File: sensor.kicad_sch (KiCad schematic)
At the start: 135 parts, among them IC1 A3909, J1 Micro_SD_Card_Det1, J12 Conn_01x04, J13 1x3 servo, J14 1x3 servo, J15 arming terminal, J16 arming terminal, J17 arming terminal, J18 arming terminal, J19 Screw_Terminal_01x02, J20 Screw_Terminal_01x02, J21 Screw_Terminal_01x02, J22 Screw_Terminal_01x02, J3 Conn_Coaxial, J4 H9161TR-ND, J5 Screw_Term, J6 1x3 servo, J9 1x3 servo, Q1 2N7002, Q10 2N7002, Q11 2N7002, Q12 2N7002, Q13 2N7002, Q3 2N7002, Q4 2N7002, Q5 2N7002, Q6 2N7002, Q7 BSS138, U10 LSM6DS3, U2 IMU, U5 LPS22HB, U6 GPS, U7 SX1276, U8 NAND, Y2 32.768kHz

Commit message: Added GPS footprint
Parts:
- U6: footprint L96-M33:XCVR_L96-M33 -> RF_GPS:Quectel_L96
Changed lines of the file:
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@@
 			)
 		)
-		(property "Footprint" "L96-M33:XCVR_L96-M33"
+		(property "Footprint" "RF_GPS:Quectel_L96"
 			(at 71.12 54.61 0)
 			(effects
@@
 			(at 71.12 54.61 0)
 			(effects
+				(font
+					(size 1.27 1.27)
+				)
+				(hide yes)
+			)
+		)
+		(property "Sim.Name" "<unknown>"
+			(at 71.12 54.61 0)
+			(effects

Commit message: i fogro
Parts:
- removed Q1, Q10, Q11, Q12, Q13, Q3, Q4, Q5, Q6: 2N7002, Package_TO_SOT_SMD:SOT-23, symbol Transistor_FET:2N7002
- added Q1, Q10, Q11, Q3, Q4, Q5, Q6, Q8, Q9: IRLML6402, Package_TO_SOT_SMD:SOT-23, symbol Transistor_FET:IRLML6402
- J1: footprint (none) -> Connector_Card:microSD_HC_Hirose_DM3D-SF
- J12: footprint (none) -> Connector_PinSocket_2.54mm:PinSocket_1x04_P2.54mm_Vertical
- J15, J16, J17, J18, J19, J20, J21, J22, J5: footprint (none) -> TerminalBlock_Phoenix:TerminalBlock_Phoenix_MKDS-1,5-2-5.08_1x02_P5.08mm_Horizontal
- Y2: footprint (none) -> Crystal:Crystal_SMD_0603-2Pin_6.0x3.5mm
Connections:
- net at R83.2: now also Q10.1 (G)
- net at R63.2: now also Q1.1 (G)
- net at J14.2 (Pin_2): now also Q1.2 (S)
- net at R68.2: now also Q1.3 (D)
- net at D4.1 (K), J20.1 (Pin_1): now also Q9.2 (S)
- net at R85.2: now also Q11.1 (G)
- net at D6.1 (K), J22.1 (Pin_1): now also Q11.2 (S)
- net at R61.2, R84.2: now also Q11.3 (D)
- net at R65.2: now also Q4.1 (G)
- net at J6.2 (Pin_2): now also Q4.2 (S)
- net at R70.2: now also Q4.3 (D)
- net at R64.2: now also Q3.1 (G)
- net at J13.2 (Pin_2): now also Q3.2 (S)
- net at R69.2: now also Q3.3 (D)
- net at D5.1 (K), J21.1 (Pin_1): now also Q10.2 (S)
- net at R60.2, R82.2: now also Q10.3 (D)
- net at R59.2, R80.2: now also Q9.3 (D)
- net at R66.2: now also Q5.1 (G)
- net at R67.2: now also Q6.1 (G)
- net at R79.2: now also Q8.1 (G)
- net at R71.2: now also Q5.3 (D)
- net at R62.2: now also Q6.3 (D)
- net at D3.1 (K), J19.1 (Pin_1): now also Q8.2 (S)
- net at R58.2, R78.2: now also Q8.3 (D)
- net at R81.2: now also Q9.1 (G)
- net at 1x3servo1.2 (Pin_2): now also Q6.2 (S)
- net at J9.2 (Pin_2): now also Q5.2 (S)

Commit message: started pcb
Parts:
- C14, C15, C18, C19, C20, C21, C22, C23, C24, C25, C26, C44, C45, C46, C47, C48, C49, C50, C51, C52, C53, C54, C55, C56, C57, C58: footprint Capacitor_SMD:C_0201_0603Metric -> Capacitor_SMD:C_0603_1608Metric
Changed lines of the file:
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@@
 			)
 		)
-		(property "Footprint" "Capacitor_SMD:C_0201_0603Metric"
+		(property "Footprint" "Capacitor_SMD:C_0603_1608Metric"
 			(at 116.84 145.0848 0)
 			(effects
@@
 			)
 		)
-		(property "Footprint" "Capacitor_SMD:C_0201_0603Metric"
+		(property "Footprint" "Capacitor_SMD:C_0603_1608Metric"
 			(at 342.9 32.7152 0)
 			(effects
@@
 			)
 		)
-		(property "Footprint" "Capacitor_SMD:C_0201_0603Metric"
+		(property "Footprint" "Capacitor_SMD:C_0603_1608Metric"
 			(at 116.84 134.9248 0)
 			(effects
@@
 			)
 		)
-		(property "Footprint" "Capacitor_SMD:C_0201_0603Metric"
+		(property "Footprint" "Capacitor_SMD:C_0603_1608Metric"
 			(at 91.44 117.1448 0)
 			(effects
@@
 			)
 		)
-		(property "Footprint" "Capacitor_SMD:C_0201_0603Metric"
+		(property "Footprint" "Capacitor_SMD:C_0603_1608Metric"
 			(at -2.2352 175.26 0)
 			(effects
@@
 			)
 		)
-		(property "Footprint" "Capacitor_SMD:C_0201_0603Metric"
+		(property "Footprint" "Capacitor_SMD:C_0603_1608Metric"
 			(at 37.7952 165.1 0)
 			(effects
@@
 			)
 		)
-		(property "Footprint" "Capacitor_SMD:C_0201_0603Metric"
+		(property "Footprint" "Capacitor_SMD:C_0603_1608Metric"
 			(at 91.44 120.3452 0)
 			(effects
@@
 			)
 		)
-		(property "Footprint" "Capacitor_SMD:C_0201_0603Metric"
+		(property "Footprint" "Capacitor_SMD:C_0603_1608Metric"
 			(at 270.51 36.83 0)
 			(effects
@@
 			)
 		)
-		(property "Footprint" "Capacitor_SMD:C_0201_0603Metric"
+		(property "Footprint" "Capacitor_SMD:C_0603_1608Metric"
 			(at 105.1052 34.29 0)
 			(effects
@@
 			)
 		)
-		(property "Footprint" "Capacitor_SMD:C_0201_0603Metric"
+		(property "Footprint" "Capacitor_SMD:C_0603_1608Metric"
 			(at 280.67 39.37 0)
 			(effects
@@
 			)
 		)
-		(property "Footprint" "Capacitor_SMD:C_0201_0603Metric"
+		(property "Footprint" "Capacitor_SMD:C_0603_1608Metric"
 			(at 193.04 127.3048 0)
 			(effects
@@
 			)
 		)
-		(property "Footprint" "Capacitor_SMD:C_0201_0603Metric"
+		(property "Footprint" "Capacitor_SMD:C_0603_1608Metric"
 			(at 91.44 122.2248 0)
 			(effects
@@
 			)
 		)
-		(property "Footprint" "Capacitor_SMD:C_0201_0603Metric"
+		(property "Footprint" "Capacitor_SMD:C_0603_1608Metric"
 			(at 266.3952 27.94 0)
 			(effects
@@
 			)
 		)
-		(property "Footprint" "Capacitor_SMD:C_0201_0603Metric"
+		(property "Footprint" "Capacitor_SMD:C_0603_1608Metric"
 			(at 229.87 89.8652 0)
 			(effects
@@
 			)
 		)
-		(property "Footprint" "Capacitor_SMD:C_0201_0603Metric"
+		(property "Footprint" "Capacitor_SMD:C_0603_1608Metric"
 			(at 229.87 84.7852 0)
 			(effects
@@
 			)
 		)
-		(property "Footprint" "Capacitor_SMD:C_0201_0603Metric"
+		(property "Footprint" "Capacitor_SMD:C_0603_1608Metric"
 			(at 91.44 125.4252 0)
 			(effects
@@
 			)
 		)
-		(property "Footprint" "Capacitor_SMD:C_0201_0603Metric"
+		(property "Footprint" "Capacitor_SMD:C_0603_1608Metric"
 			(at 93.98 42.8752 0)
 			(effects
@@
 			)
 		)
-		(property "Footprint" "Capacitor_SMD:C_0201_0603Metric"
+		(property "Footprint" "Capacitor_SMD:C_0603_1608Metric"
 			(at 127.3048 160.02 0)
 			(effects
@@
 			)
 		)
-		(property "Footprint" "Capacitor_SMD:C_0201_0603Metric"
+		(property "Footprint" "Capacitor_SMD:C_0603_1608Metric"
 			(at 114.3 159.0548 0)
 			(effects
@@
 			)
 		)
-		(property "Footprint" "Capacitor_SMD:C_0201_0603Metric"
+		(property "Footprint" "Capacitor_SMD:C_0603_1608Metric"
 			(at 340.36 30.7848 0)
 			(effects
@@
 			)
 		)
-		(property "Footprint" "Capacitor_SMD:C_0201_0603Metric"
+		(property "Footprint" "Capacitor_SMD:C_0603_1608Metric"
 			(at 262.89 51.7652 0)
 			(effects
@@
 			)
 		)
-		(property "Footprint" "Capacitor_SMD:C_0201_0603Metric"
+		(property "Footprint" "Capacitor_SMD:C_0603_1608Metric"
 			(at 271.4752 27.94 0)
 			(effects
@@
 			)
 		)
-		(property "Footprint" "Capacitor_SMD:C_0201_0603Metric"
+		(property "Footprint" "Capacitor_SMD:C_0603_1608Metric"
 			(at 116.84 140.0048 0)
 			(effects
@@
 			)
 		)
-		(property "Footprint" "Capacitor_SMD:C_0201_0603Metric"
+		(property "Footprint" "Capacitor_SMD:C_0603_1608Metric"
 			(at 91.44 115.2652 0)
 			(effects
@@
 			)
 		)
-		(property "Footprint" "Capacitor_SMD:C_0201_0603Metric"
+		(property "Footprint" "Capacitor_SMD:C_0603_1608Metric"
 			(at 117.8052 36.83 0)
 			(effects
@@
 			)
 		)
-		(property "Footprint" "Capacitor_SMD:C_0201_0603Metric"
+		(property "Footprint" "Capacitor_SMD:C_0603_1608Metric"
 			(at 116.84 150.1648 0)
 			(effects

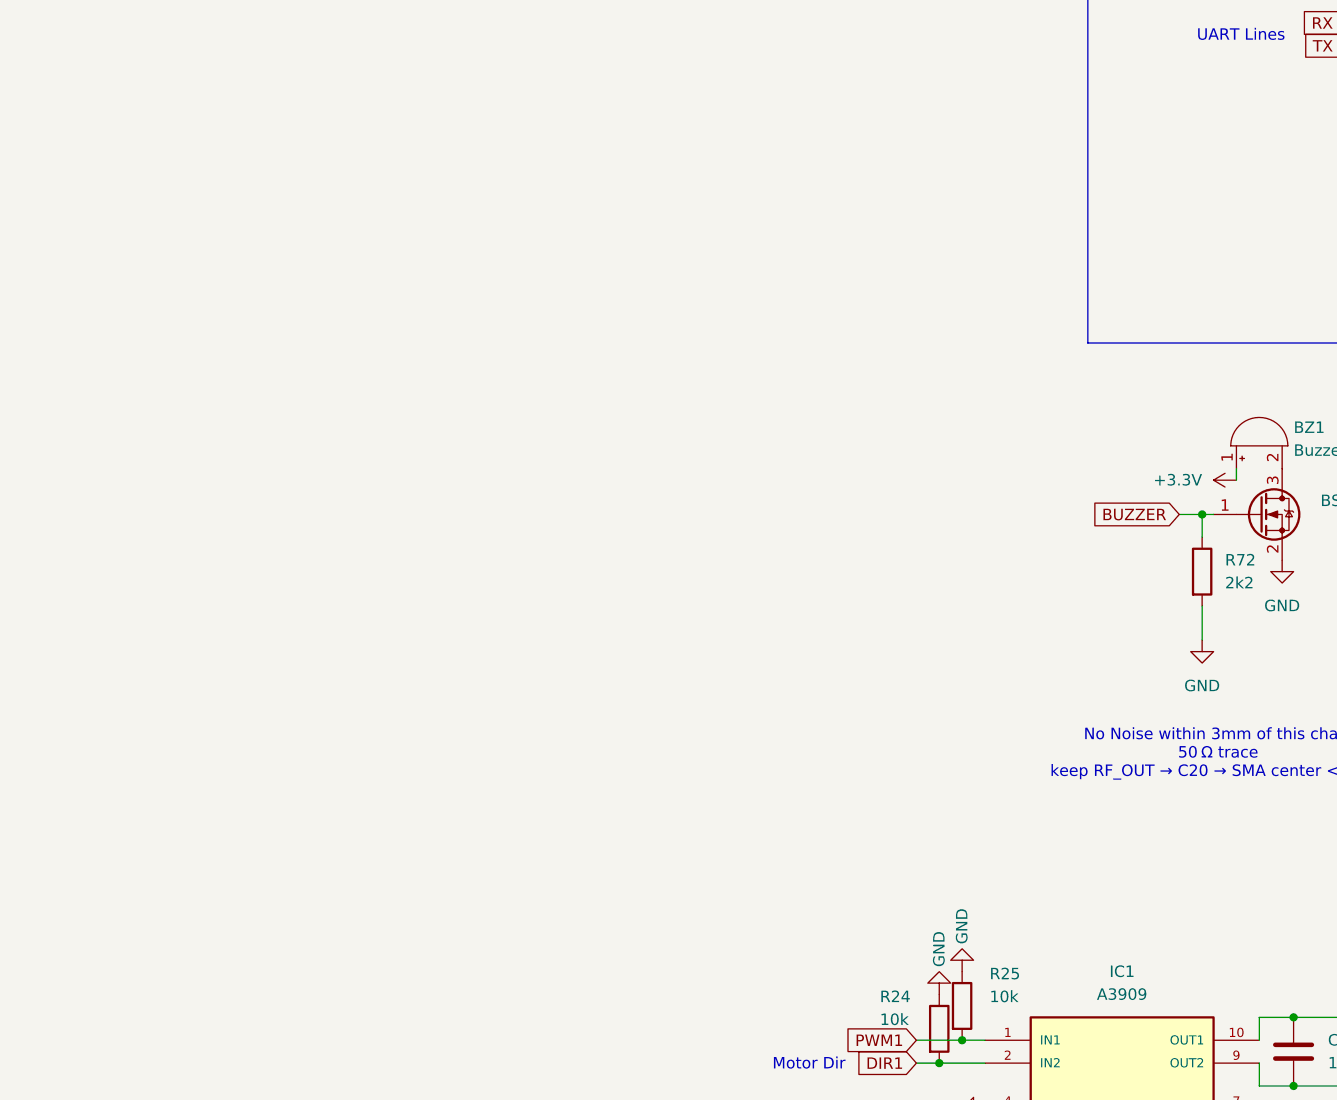
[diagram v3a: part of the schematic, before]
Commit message: Hopefully added BL, and all the remaining footprints
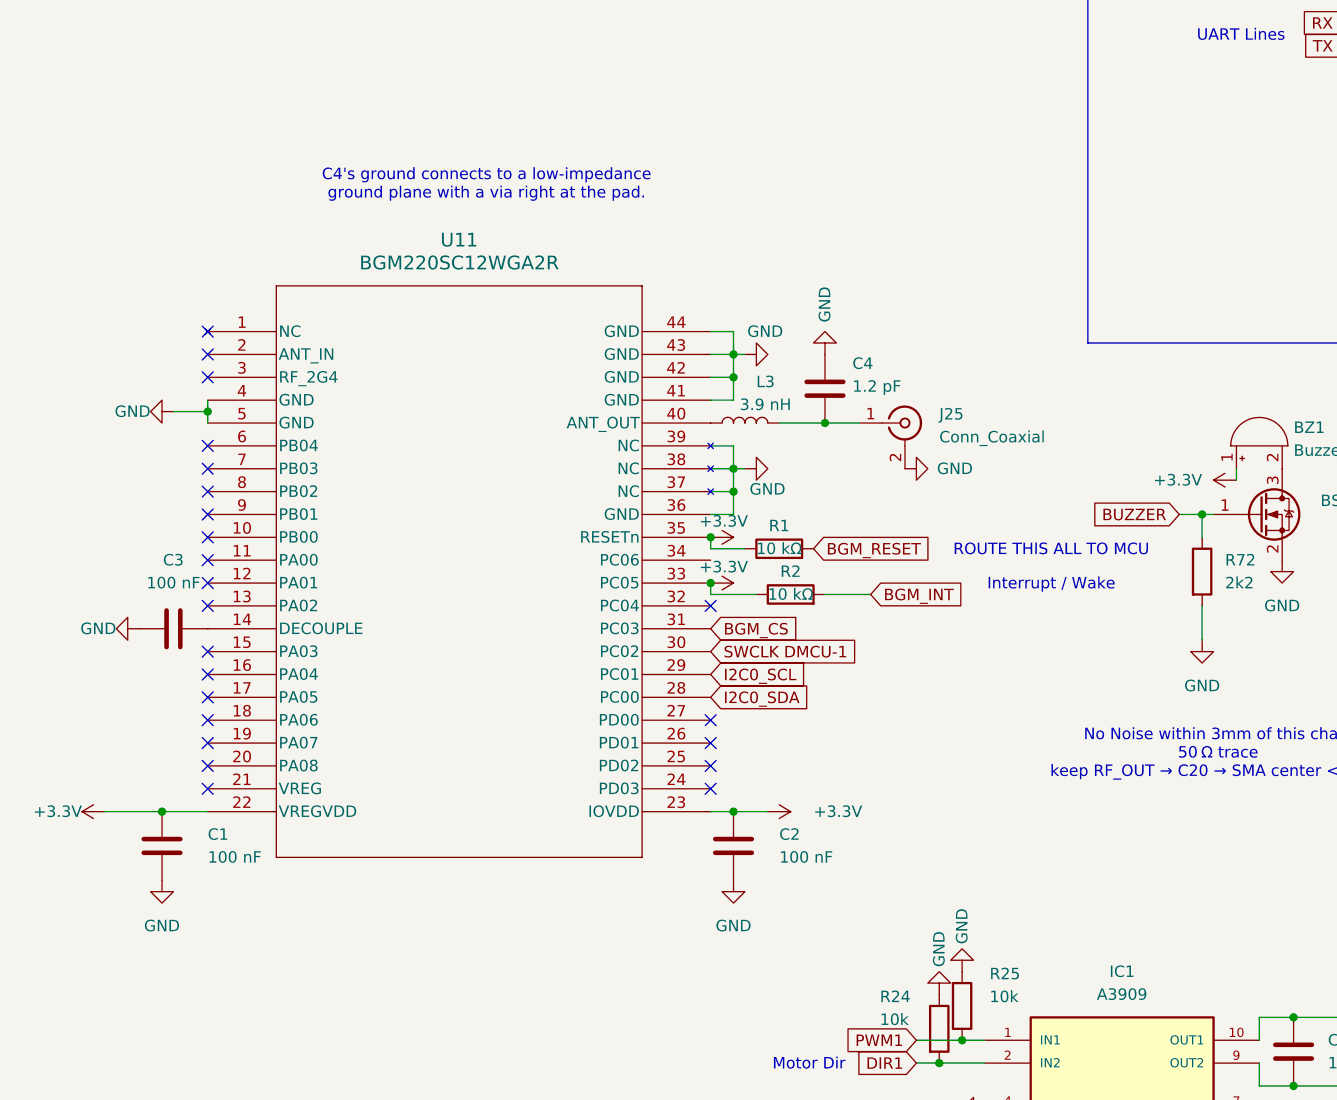
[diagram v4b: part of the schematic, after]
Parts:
- added C1, C2, C3: 100 nF, Capacitor_SMD:C_0603_1608Metric, symbol Device:C
- added C4: 1.2 pF, symbol Device:C
- added J25: Conn_Coaxial, SMA:LPRS_SMA_CONNECTOR, symbol Connector:Conn_Coaxial
- added L3: 3.9 nH, symbol Device:L
- added R1, R2: 10 kΩ, Resistor_SMD:R_0603_1608Metric, symbol Device:R
- added U11: BGM220SC12WGA2R, BGM220S_SIL:BGM220SC12WGA2R, symbol 2025-05-18_04-09-44:BGM220SC12WGA2R
- J3: footprint (none) -> SMA:LPRS_SMA_CONNECTOR
- J4: footprint (none) -> U.FL:HRS_U.FL-R-SMT_01_
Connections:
- net +3.3V: now also C1.2, C2.2, R1.1, R2.1, U11.22 (VREGVDD), U11.23 (IOVDD), U11.33 (PC05), U11.35 (RESETn)
- net GND: now also C1.1, C2.1, C3.1, C4.1, J25.2 (Ext), U11.36 (GND), U11.37 (NC), U11.38 (NC), U11.39 (NC), U11.4 (GND), U11.41 (GND), U11.42 (GND), U11.43 (GND), U11.44 (GND), U11.5 (GND)
- new net: C4.2, J25.1 (In), L3.2
- new net: L3.1, U11.40 (ANT_OUT)
- new net: C3.2, U11.14 (DECOUPLE)
- new net BGM_CS: U11.31 (PC03)
- new net BGM_INT: R2.2
- new net BGM_RESET: R1.2
- new net I2C0_SCL: U11.29 (PC01)
- new net I2C0_SDA: U11.28 (PC00)
- new net SWCLK DMCU-1: U11.30 (PC02)
- no-connect marks 32 -> 55
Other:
- note added: "C4's ground connects to a low-impedance ground plane with a via right at the pad."
- note added: "Interrupt / Wake"
- note added: "ROUTE THIS ALL TO MCU"
